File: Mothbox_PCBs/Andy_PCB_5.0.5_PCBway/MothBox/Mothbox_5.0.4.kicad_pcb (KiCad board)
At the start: 2 copper layers, 237 x 139 mm, 182 parts, among them J1 DB141V-2.54-4P, J2 DB141V-2.54-4P, J3 DB141V-2.54-4P, J4 DB141V-2.54-4P, J5 Conn_1.25mm, Q1 AP30P30Q, Q10 AP30P30Q, Q13 AP30P30Q, Q2 AO3400A, Q3 YJQ10N2A, Q4 YJQ10N2A, Q5 YJQ10N2A, Q6 YJQ10N2A, Q7 YJQ10N2A, Q8 AP30P30Q, Q9 YJQ10N2A, SW2 KH-6X6X5H-STM, U10 Days, U11 Hours3, U12 MODE, U13 Hours1, U14 Hours2, U15 PCA9555PW, U16 PCA9555PW, U17 DS18B20U, U18 LTR-303ALS-01, U19 graphic, U2 XL4015E1, U3 INA219BIDCNT, U5 RASPBERRY_PI_5, U6 RASPBERRY_PI_4B_4GB, U7 Female Inv Socket Pi 2.54-2*20, U8 GPs 5 pin PM2.54-1*5, U9 PCA9555PW

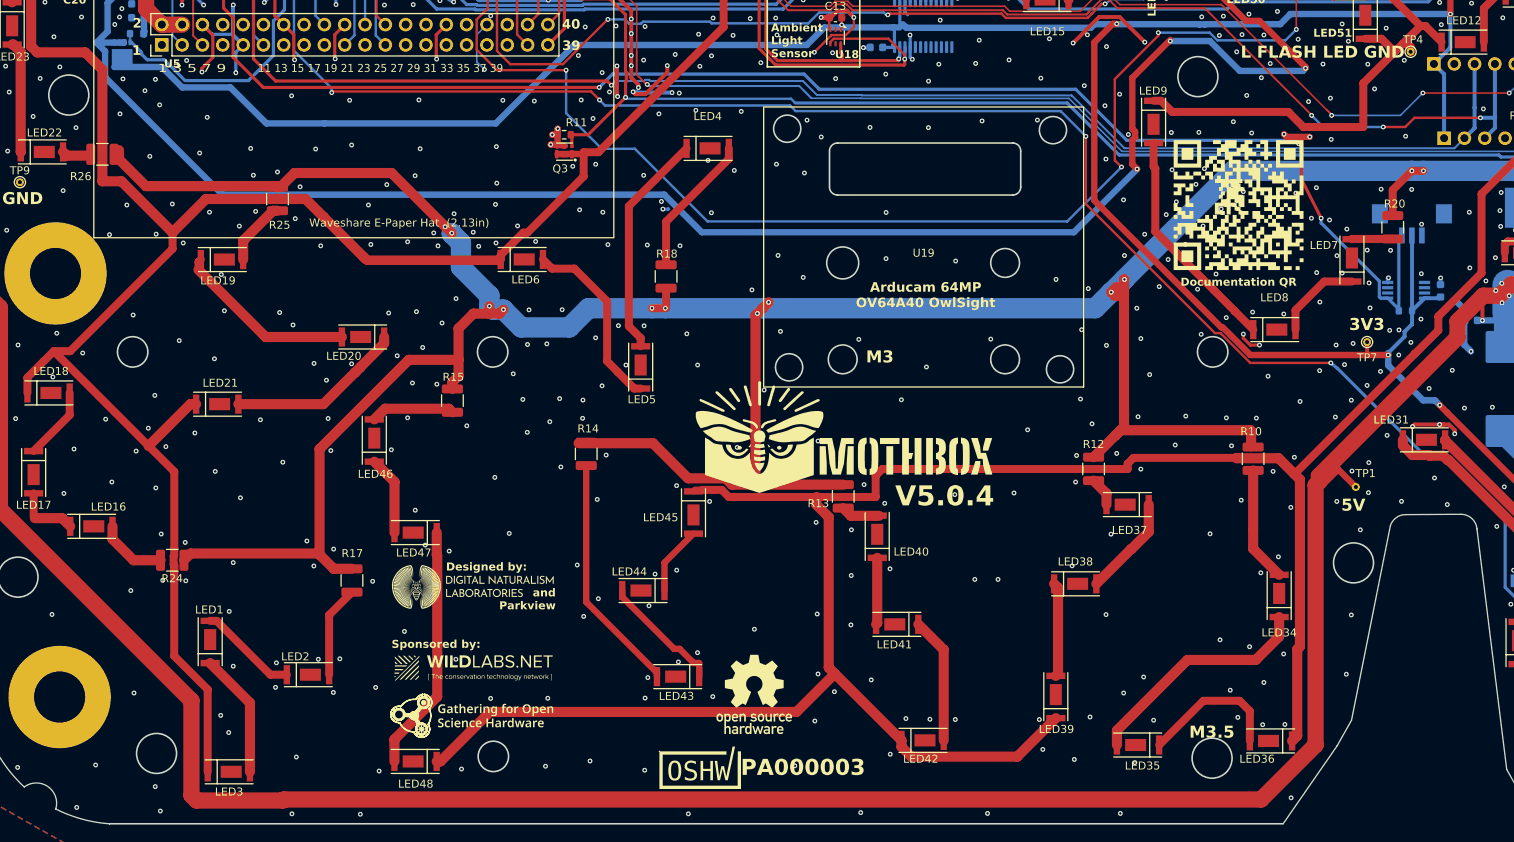
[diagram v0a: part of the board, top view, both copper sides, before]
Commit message: made PCBway pcb v5.0.5
Major Changes:
Done: Added second set of holes for mounting battery
Done: added highlights on battery mounting holes
Done: added PCBway logo for pcb sponsorship
Done: Changed labelling on switches to make them confuse JLC people less
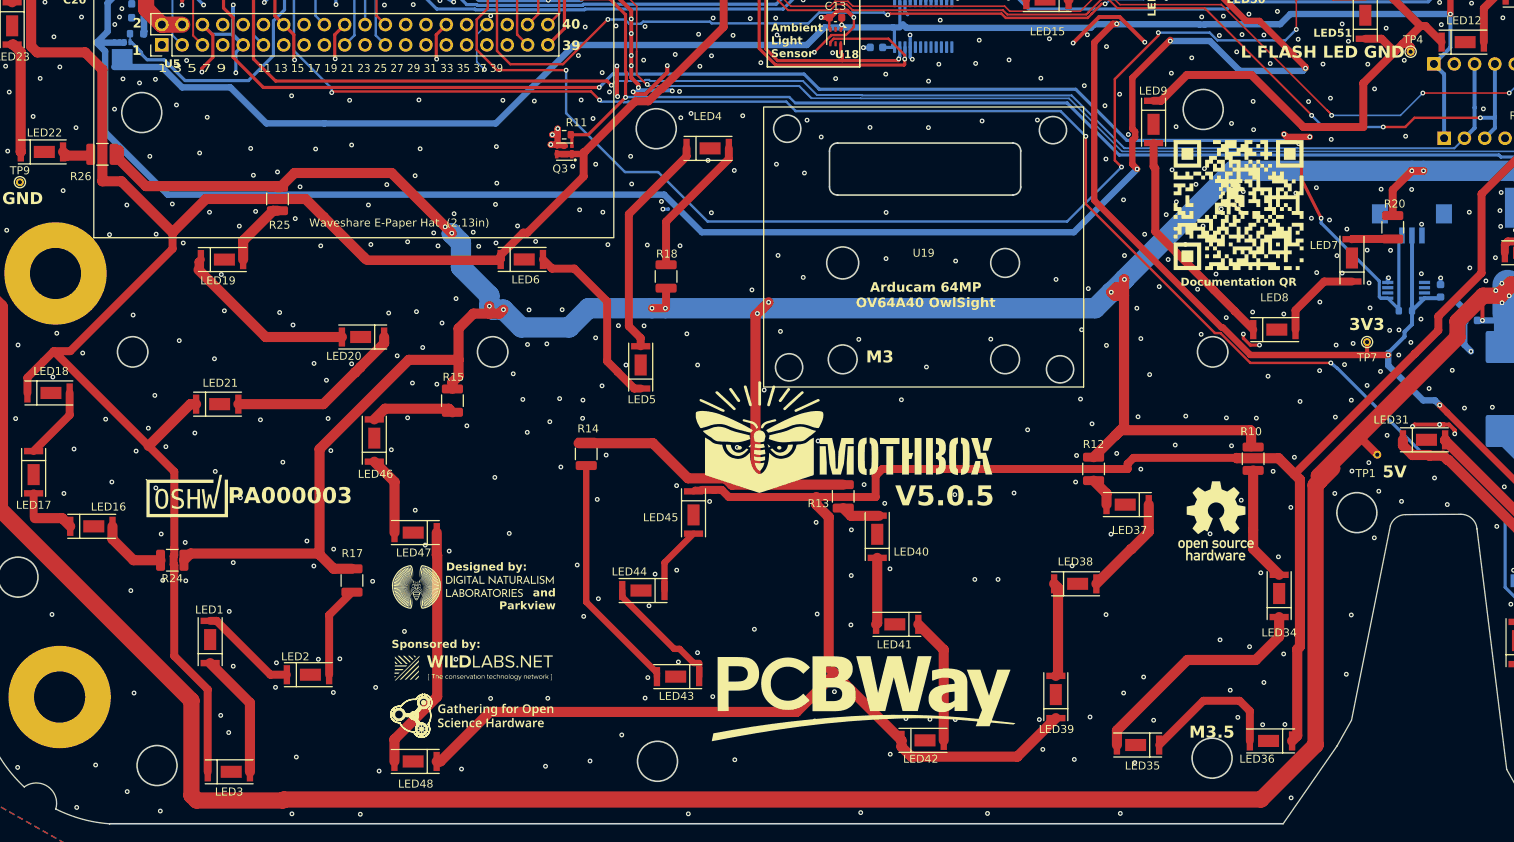
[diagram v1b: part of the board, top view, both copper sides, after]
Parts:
- moved TP1 4.85 mm to (206.9, 111.8)
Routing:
- net +3V3: track 231.3 -> 235.3 mm
- net Net-(LED12-K): track 451.0 -> 453.7 mm
- net GND: track 437.2 -> 437.3 mm, vias 926 -> 927
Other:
- outline, holes or cut-outs redrawn
- board text added: "--------DAYS-----"
- board text added: "Active"
- board text added: "Documentation: www.mothbox.org"
- board text added: "MOTHBOX V5.0.5"
- board text added: "Mo Tu We Th Fr Sa Su"
- board text added: "V5.0.5"
- board text removed: "--------DAYS---------"
- board text removed: "Documentation: https://digital-naturalism-laboratories.github.io/Mothbox/"
- board text removed: "MOTHBOX V5.0.4"
- board text removed: "Mo Tu We Th Fr Sa Su Active"
- board text removed: "V5.0.4"

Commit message: added "On" signifiers for switches
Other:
- board text added: "On"
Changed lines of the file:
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@@
 	(gr_poly
 		(pts
-			(xy 249.64 21.275671) (xy 249.72016 32.030644) (xy 170.875876 32.030644) (xy 170.771001 21.377167)
+			(xy 249.466952 21.275894) (xy 249.54711 32.030644) (xy 171.784982 32.030644) (xy 171.680095 21.375998)
 		)
 		(stroke
@@
 		)
 	)
+	(gr_text "On"
+		(at 226.79 20.785671 0)
+		(layer "B.SilkS")
+		(effects
+			(font
+				(size 0.6 0.6)
+				(thickness 0.075)
+			)
+			(justify mirror)
+		)
+	)
 	(gr_text "(9-36v)"
 		(at 228.733836 148.968599 270)
@@
 		)
 	)
+	(gr_text "On"
+		(at 161.1 43.915671 0)
+		(layer "B.SilkS")
+		(effects
+			(font
+				(size 0.6 0.6)
+				(thickness 0.075)
+			)
+			(justify mirror)
+		)
+	)
 	(gr_text "3V3"
 		(at 207.44117 100.723018 0)
@@
 		)
 	)
+	(gr_text "On"
+		(at 248.08 20.785671 0)
+		(layer "B.SilkS")
+		(effects
+			(font
+				(size 0.6 0.6)
+				(thickness 0.075)
+			)
+			(justify mirror)
+		)
+	)
 	(gr_text "M3.5"
 		(at 49.04 70.045671 0)
@@
 		)
 	)
+	(gr_text "On"
+		(at 193.14 20.755671 0)
+		(layer "B.SilkS")
+		(effects
+			(font
+				(size 0.6 0.6)
+				(thickness 0.075)
+			)
+			(justify mirror)
+		)
+	)
 	(gr_text "M3"
 		(at 169.020333 98.387038 0)
@@
 			)
 			(justify mirror)
+		)
+	)
+	(gr_text "On"
+		(at 170.67 23.495671 0)
+		(layer "B.SilkS")
+		(effects
+			(font
+				(size 0.6 0.6)
+				(thickness 0.075)
+			)
+			(justify mirror)
